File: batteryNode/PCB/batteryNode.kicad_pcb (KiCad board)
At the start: 2 copper layers, 62.2 x 27.9 mm, 51 parts, among them J100 cell_taps, J101 therm_conn, J200 ISP_Header, J300 Conn_01x06, Q100 IRLML9303TRPBF, SW200 SW_Push, U100 BQ76925RGER, U200 ATtiny2313A-MU, U300 LTC2875-DD, Y200 10MHz

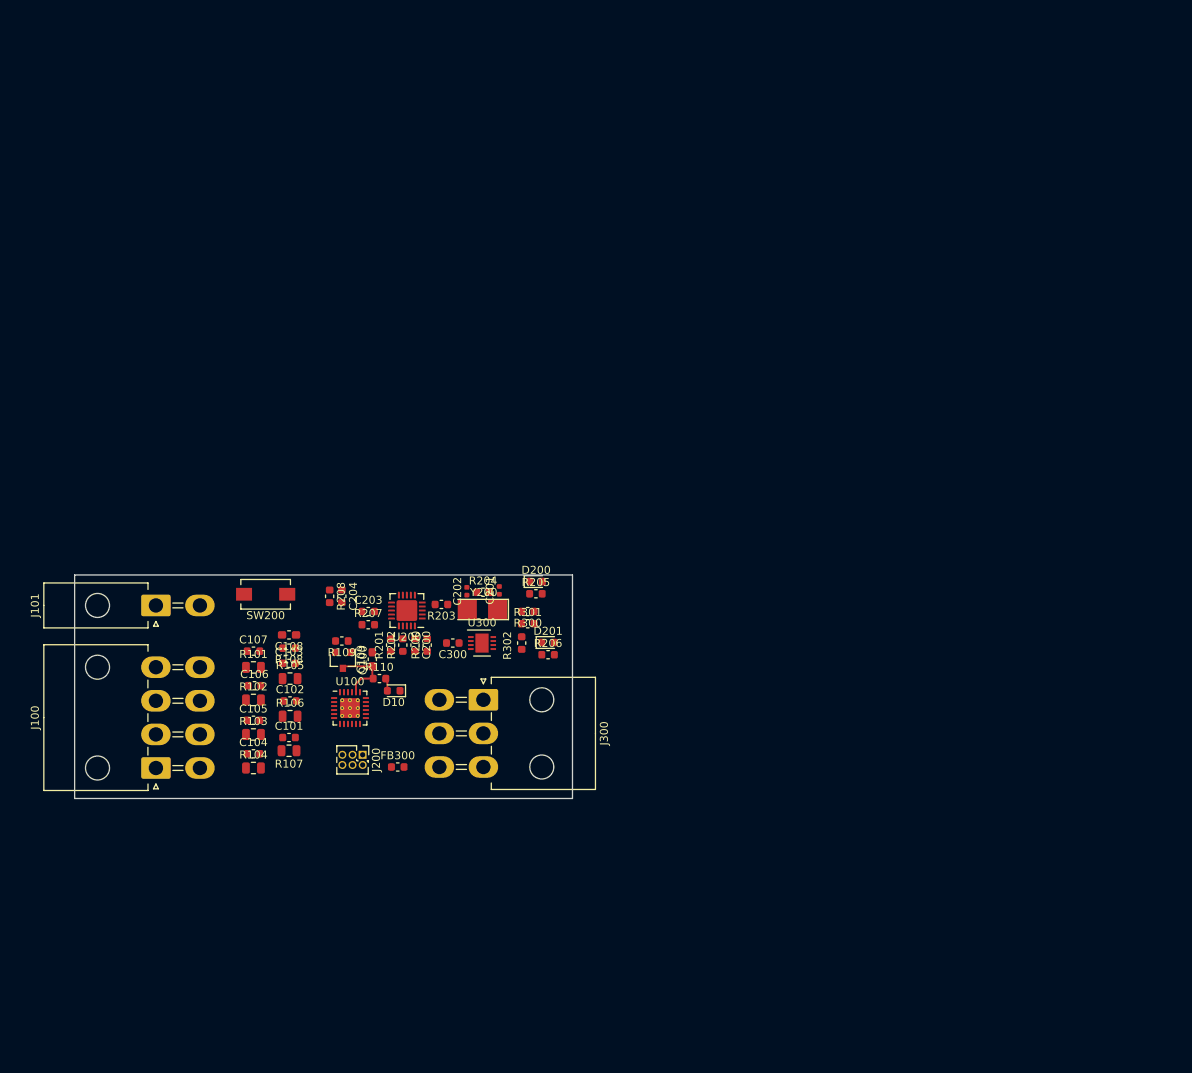
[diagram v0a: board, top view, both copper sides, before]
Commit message: Restarted Layout and added logos and mounting holes to schematic
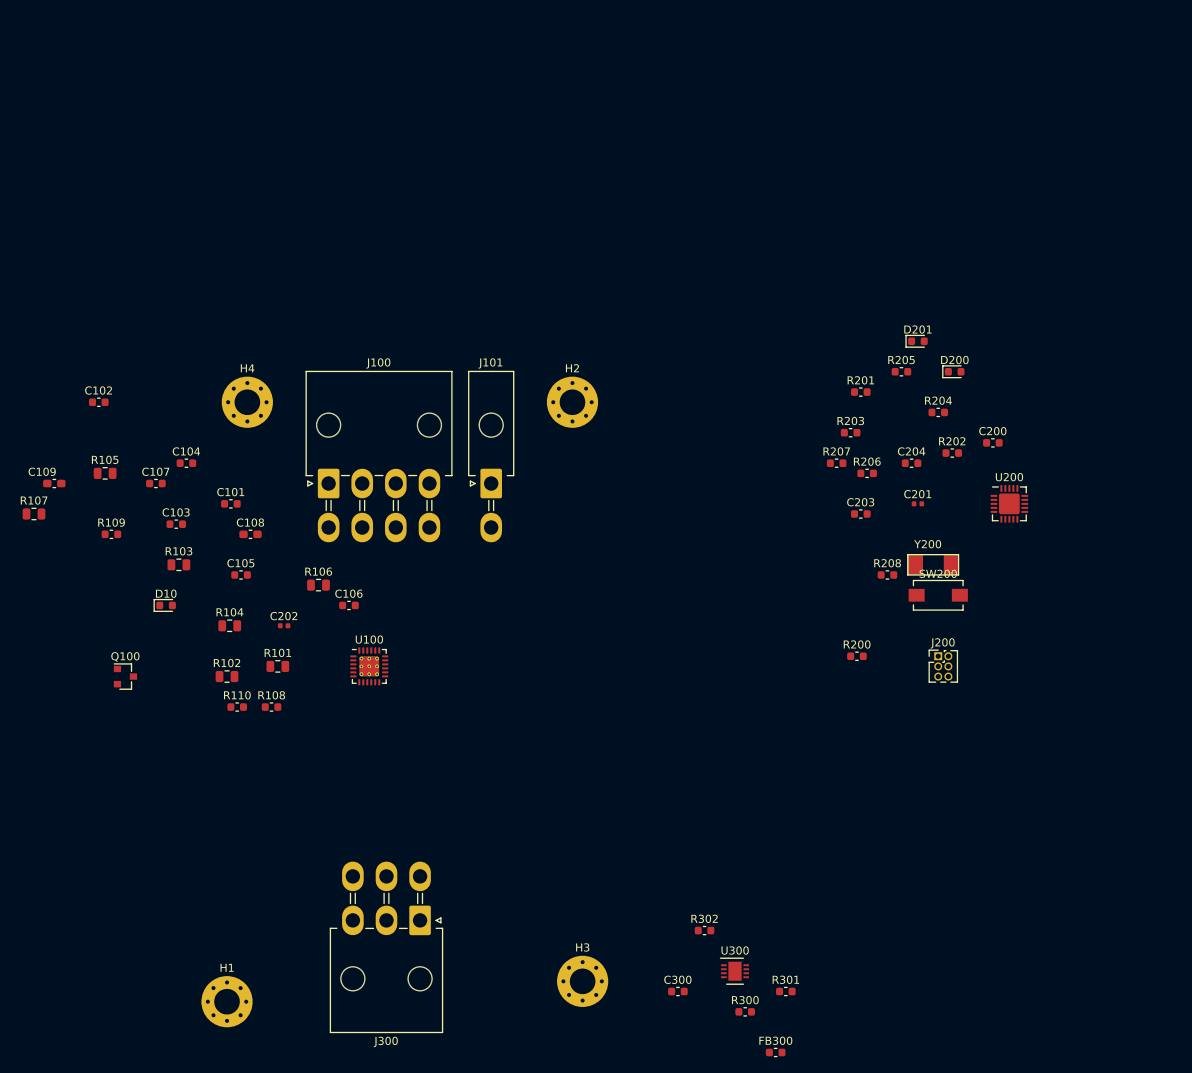
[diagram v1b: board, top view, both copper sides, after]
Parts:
- added H1: MountingHole, MountingHole:MountingHole_3.2mm_M3_Pad_Via, F.Cu at (64.8, 156.2)
- added H2: MountingHole, MountingHole:MountingHole_3.2mm_M3_Pad_Via, F.Cu at (108.0, 81.3)
- added H3: MountingHole, MountingHole:MountingHole_3.2mm_M3_Pad_Via, F.Cu at (109.2, 153.7)
- added H4: MountingHole, MountingHole:MountingHole_3.2mm_M3_Pad_Via, F.Cu at (67.3, 81.3)
- moved SW200 84.1 mm to (153.7, 105.4), turned to 0 degrees
- moved C200 76.5 mm to (160.5, 86.4), turned to 0 degrees
- moved U200 76.5 mm to (162.6, 94.0), turned to 0 degrees
- moved C204 73.1 mm to (150.3, 88.9), turned to 0 degrees
- moved J200 73.0 mm to (153.7, 113.0), turned to 0 degrees
- moved R202 72.8 mm to (155.4, 87.6), turned to 0 degrees
- moved R208 69.8 mm to (147.3, 102.9), turned to 0 degrees
- moved R201 66.7 mm to (144.0, 80.0), turned to 0 degrees
- moved C203 62.8 mm to (144.0, 95.2)
- moved R207 61.9 mm to (141.0, 88.9)
- moved R204 61.2 mm to (153.7, 82.5)
- moved D201 59.6 mm to (151.1, 73.7)
- moved FB300 59.2 mm to (133.3, 162.6)
- moved D200 58.5 mm to (155.7, 77.5)
- moved R300 56.9 mm to (129.5, 157.5), turned to 0 degrees
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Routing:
- net +3V3: track 8.83 -> 0.00 mm
- net Net-(D10-Pad2): track 1.61 -> 0.00 mm
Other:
- board outline removed

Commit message: added current control. Started V2 of layout
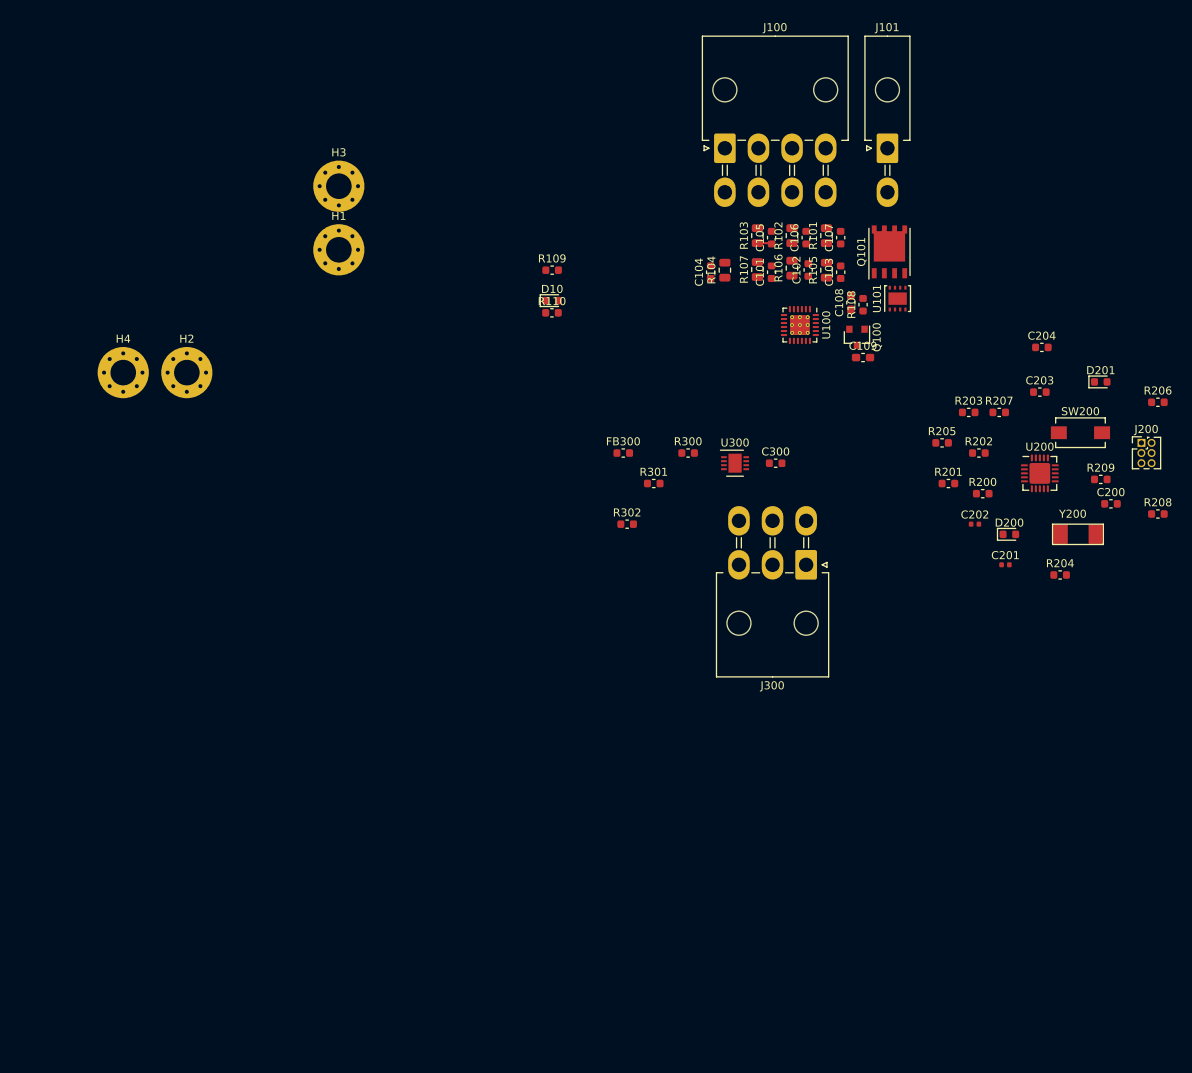
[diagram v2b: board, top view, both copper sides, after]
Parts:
- added Q101: NMOS, Package_SO:PowerPAK_SO-8_Single, F.Cu at (147.6, 62.5)
- added R209: 10k, Resistor_SMD:R_0603_1608Metric, F.Cu at (174.0, 90.9)
- added U101: MIC5060, Package_DFN_QFN:MLF-8-1EP_3x3mm_P0.65mm_EP1.55x2.3mm, F.Cu at (148.6, 68.3)
- J101: value therm_conn -> load
- moved H3 104.0 mm to (78.7, 54.3)
- moved C109 102.3 mm to (144.3, 75.7)
- moved Q100 100.8 mm to (143.5, 73.2), turned to 270 degrees
- moved R107 95.4 mm to (131.1, 64.7), turned to 90 degrees
- moved H1 95.0 mm to (78.7, 62.2)
- moved R105 93.7 mm to (139.7, 64.8), turned to 90 degrees
- moved C107 90.9 mm to (141.5, 60.7), turned to 90 degrees
- moved C102 90.2 mm to (137.4, 64.7), turned to 90 degrees
- moved R102 89.6 mm to (135.4, 60.5), turned to 90 degrees
- moved R108 89.4 mm to (144.3, 69.1), turned to 90 degrees
- moved C103 88.8 mm to (141.5, 65.0), turned to 90 degrees
- moved C202 87.3 mm to (158.3, 96.5)
- moved R101 87.2 mm to (139.7, 60.5), turned to 90 degrees
- moved R103 83.2 mm to (131.1, 60.5), turned to 90 degrees
- moved C108 80.4 mm to (142.7, 68.8), turned to 90 degrees
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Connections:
- net /therm_in_filt renamed /v_iout_filt
- J101 pad 1: /therm_in -> Net-(J101-Pad1)
- J101 pad 2: /therm_out -> GND
- R207 pad 2: /therm_in -> /v_iout
- U100 pad 14: Net-(U100-Pad14) -> /v_iout
- U100 pad 16: /therm_out -> Net-(U100-Pad16)
- U200 pad 7: Net-(U200-Pad7) -> /i_ctrl
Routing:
- net /tap4: track 0.00 -> 1.82 mm
- net GND: track 0.00 -> 1.53 mm

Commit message: finished v2 layout and V1 of edge cuts. edges too big around mounting holes
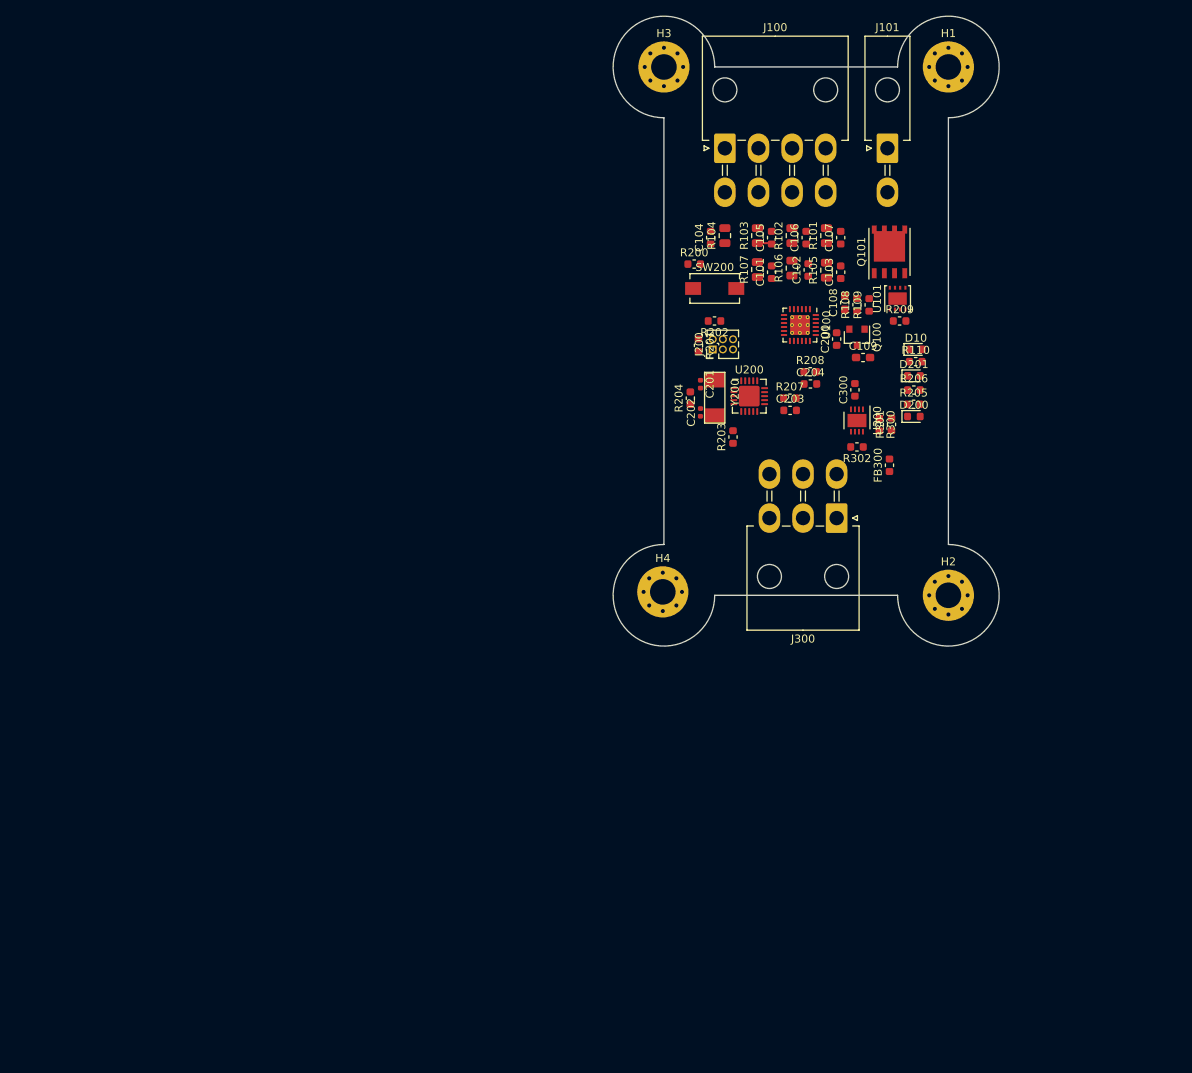
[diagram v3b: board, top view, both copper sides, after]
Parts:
- moved H2 99.2 mm to (154.9, 105.4)
- moved H1 79.5 mm to (154.9, 39.4)
- moved H4 72.8 mm to (119.2, 105.0)
- moved J200 54.9 mm to (125.5, 74.7), turned to 90 degrees
- moved R204 51.2 mm to (122.7, 80.8), turned to 90 degrees
- moved SW200 49.1 mm to (125.7, 67.1)
- moved R208 47.0 mm to (137.7, 77.5)
- moved Y200 46.8 mm to (125.7, 77.5), turned to 270 degrees
- moved R200 46.1 mm to (123.2, 64.0)
- moved D10 45.9 mm to (150.9, 74.7)
- moved R110 45.9 mm to (150.9, 76.2)
- moved C201 44.3 mm to (124.0, 79.0), turned to 270 degrees
- moved H3 43.3 mm to (119.4, 39.4)
- moved C200 40.0 mm to (141.0, 73.4), turned to 90 degrees
- moved R109 39.9 mm to (145.0, 69.1), turned to 90 degrees
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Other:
- board outline added: 48.3 x 78.7 mm

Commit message: Old changes made that I can't remember
Hopefully I don't have to roll the project back :)
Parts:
- moved D10 32.7 mm to (125.5, 95.2), turned to 180 degrees
- moved R110 32.7 mm to (125.5, 96.8), turned to 180 degrees
- moved D201 27.9 mm to (125.5, 90.2), turned to 180 degrees
- moved D200 27.2 mm to (125.5, 93.5), turned to 180 degrees
- moved R205 27.2 mm to (125.5, 91.9), turned to 180 degrees
- moved R206 26.7 mm to (125.5, 88.6), turned to 180 degrees
- moved FB300 15.5 mm to (132.5, 85.7), turned to 270 degrees
- moved H1 6.35 mm to (154.9, 45.7)
- moved H3 6.35 mm to (119.4, 45.7)
- moved H2 6.35 mm to (154.9, 99.1)
- moved H4 5.92 mm to (119.4, 99.1)
- moved R201 1.15 mm to (122.6, 74.3)
- moved R202 0.64 mm to (125.7, 70.5)
- moved C103 0.25 mm to (141.5, 64.8)
- moved C102 0.25 mm to (137.2, 64.7)
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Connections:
- J200 pad 1: /MISO_SDA -> /MISO
- J200 pad 4: /MOSI -> /MOSI_SDA
- Q101 pad 2: Net-(J101-Pad1) -> Net-(Q101-Pad2)
- Q101 pad 3: Net-(J101-Pad1) -> Net-(Q101-Pad3)
- Q101 pad 5: GND -> Net-(Q101-Pad5)
- U200 pad 2: Net-(C202-Pad1) -> Net-(C201-Pad1)
- U200 pad 3: Net-(C201-Pad1) -> Net-(C202-Pad1)
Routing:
- net /~alert: track 0.00 -> 32.3 mm, vias 0 -> 2
- net /i_ctrl: track 0.00 -> 27.4 mm
- net /MOSI_SDA: track 0.00 -> 26.9 mm, vias 0 -> 2
- net /SCK_SCL: track 0.00 -> 26.6 mm, vias 0 -> 4
- net /TXD: track 0.00 -> 20.8 mm, vias 0 -> 2
- net /~reset: track 0.00 -> 20.5 mm, vias 0 -> 1
- net Net-(J300-Pad3): track 0.00 -> 18.0 mm, vias 0 -> 1
- net /RXD: track 0.00 -> 17.3 mm, vias 0 -> 2
- net Net-(J300-Pad1): track 0.00 -> 16.6 mm, vias 0 -> 1
- net /tap3: track 0.00 -> 16.1 mm
- net Net-(J100-Pad2): track 0.00 -> 15.9 mm
- net Net-(J100-Pad4): track 0.00 -> 15.5 mm
- net Net-(J100-Pad3): track 0.00 -> 15.5 mm
- net /tap6: track 0.00 -> 13.5 mm
- net /iLED0: track 0.00 -> 12.0 mm, vias 0 -> 2
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- added copper zone on F.Cu, net /v_batt_filt
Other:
- board size 48.3 x 78.7 mm -> 48.3 x 66 mm
